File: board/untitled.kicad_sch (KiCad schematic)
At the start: 49 parts, among them Q1 AOD423, Q2 AOD423, Q3 AOD484, Q4 AOD484, Q5 AOD423, U3 BQ24610, U9 HT7533-1

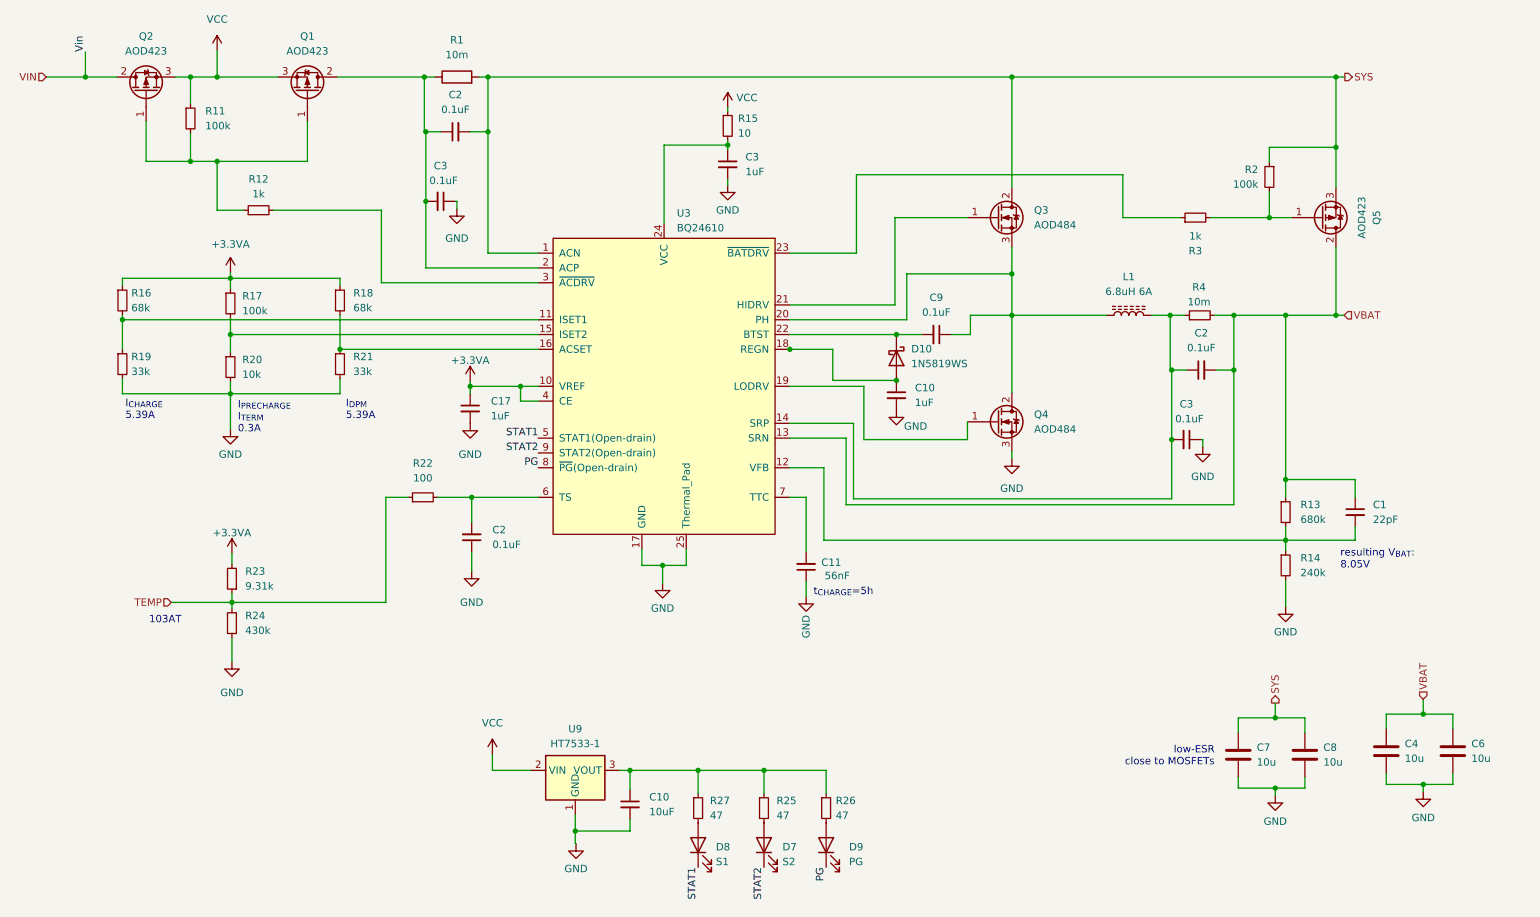
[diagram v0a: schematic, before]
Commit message: incorporate review feedback
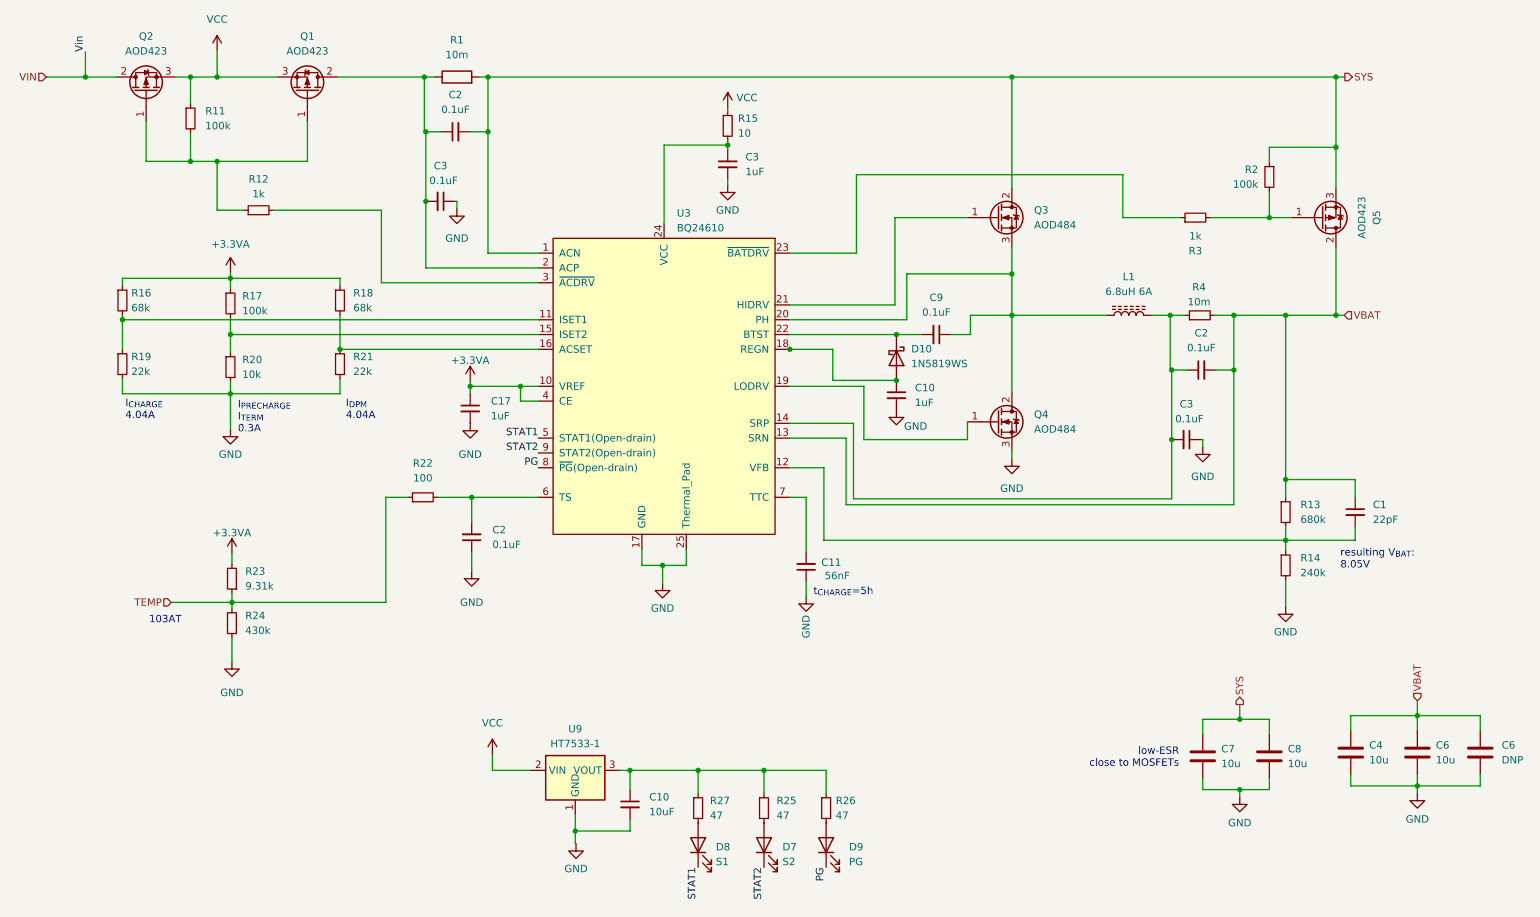
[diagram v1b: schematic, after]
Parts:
- added C6: DNP, Capacitor_SMD:C_0805_2012Metric, symbol Device:C
- R19, R21: value 33k -> 22k
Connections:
- net GND: now also C6.2
- net VBAT: now also C6.1
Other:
- note added: "I_{CHARGE} 4.04A"
- note added: "I_{DPM} 4.04A"
- note removed: "I_{CHARGE} 5.39A"
- note removed: "I_{DPM} 5.39A"
- moved on the sheet: C4, C6, C7, C8
